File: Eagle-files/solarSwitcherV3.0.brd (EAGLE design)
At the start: 46.8 x 66.2 mm, 17 parts, among them T1 2N3440

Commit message: Started on version 3.0
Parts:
- added OK1: H11L1M, optocoupler:DIL06
- R1: value 10k -> 100k
- moved D2 52.8 mm to (32.2, 58.3), turned to 315 degrees
- moved U$5 1.75 mm to (19.1, 42.0)
- turned C1 to 90 degrees
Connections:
- removed net N$10: C1.-, GREEN_LED.K, JP2.GND, JP4.4, SV2.2, T1.1, U$5.IN
- new net N$15: C1.-, D1.A, GREEN_LED.K, JP2.GND, JP3.GND, JP4.4, SV2.2, T1.1, U$2.COIL1, U$5.IN
- new net N$17: D1.C, OK1.4, U$2.COIL0
- net N$12: now also OK1.1, OK1.5; no longer D1.C, U$2.COIL0
- net N$3: no longer D1.A, U$2.COIL1
- net VCC: now also OK1.6
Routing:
- net N$15: track 0.00 -> 107.4 mm
- net N$12: track 31.6 -> 2.65 mm
- net N$17: track 0.00 -> 20.8 mm
- net N$8: track 0.00 -> 18.3 mm
- net N$1: track 35.2 -> 37.0 mm

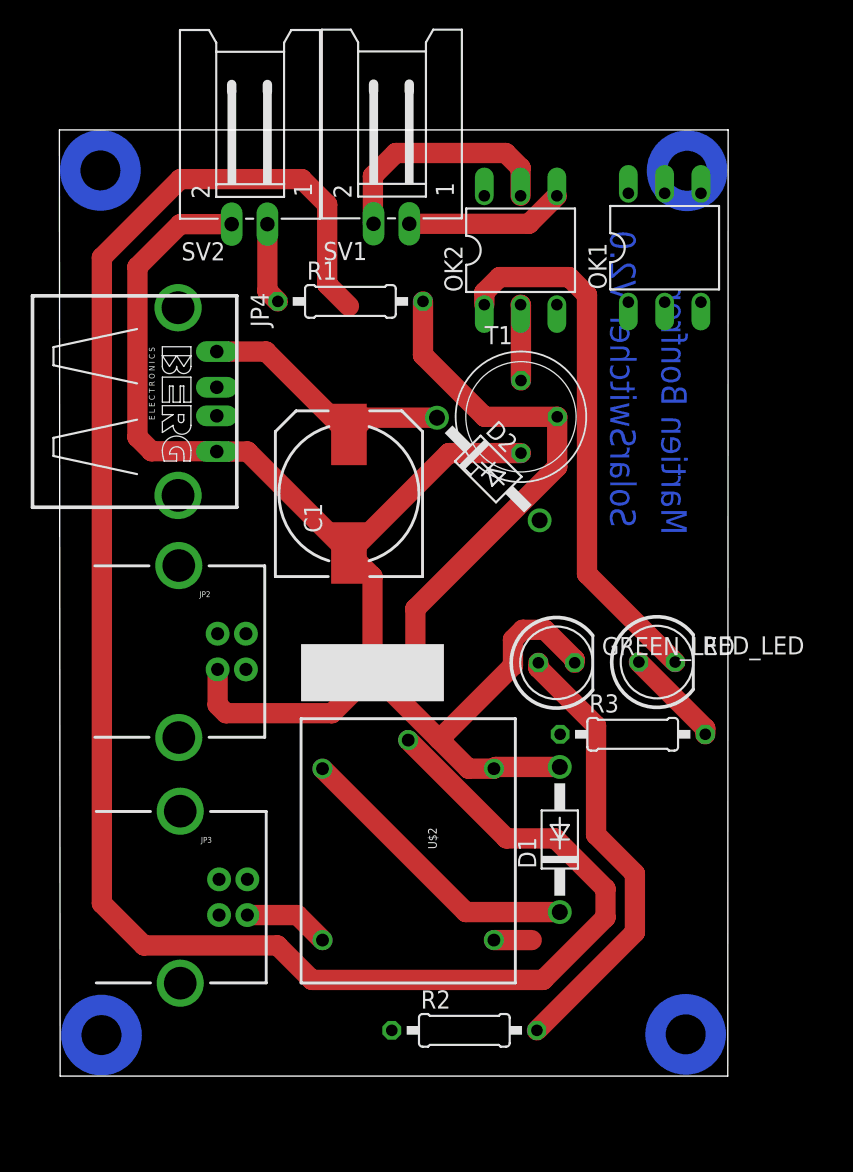
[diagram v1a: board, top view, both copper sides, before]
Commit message: Placed and connected all components
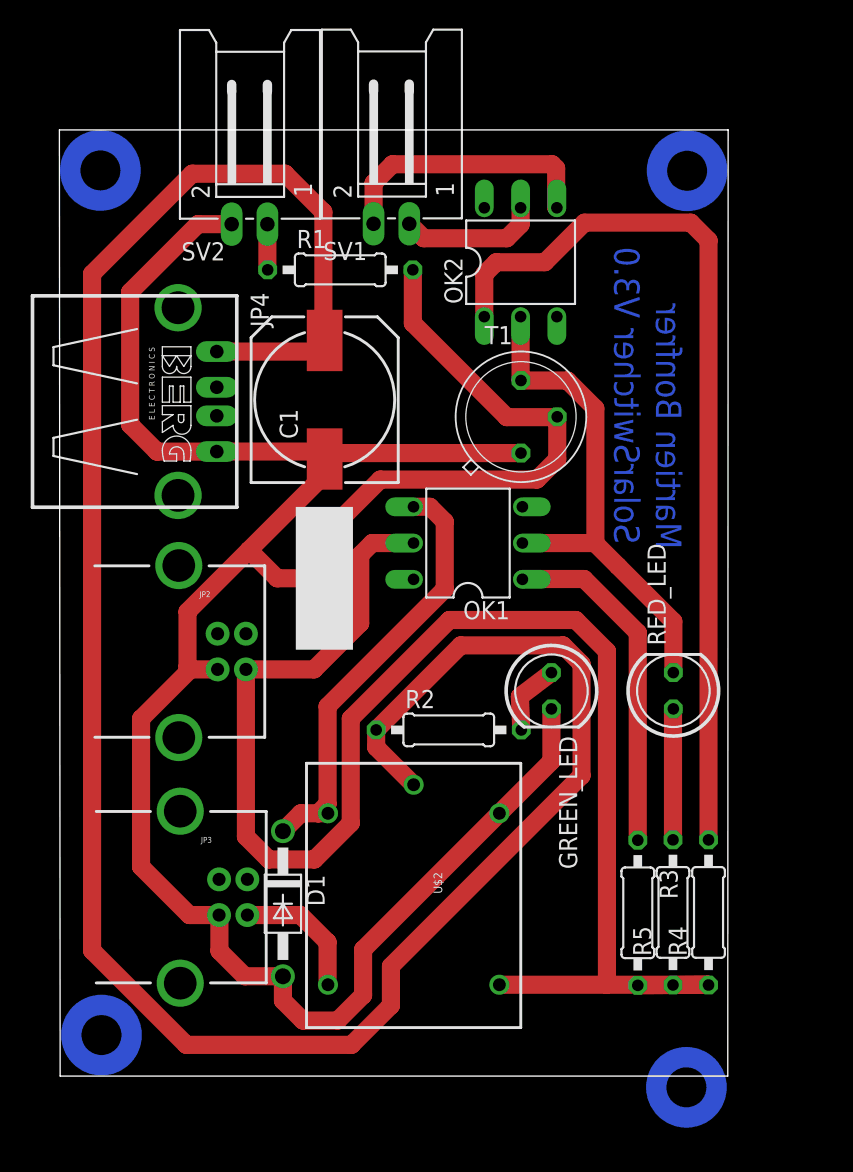
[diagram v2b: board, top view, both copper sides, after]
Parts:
- removed D2: 1N4004, diode:DO41-10
- added R4: 330, resistor:0207/10
- added R5: 150, resistor:0207/10
- R3: value 180 -> 330
- moved OK1 24.8 mm to (30.8, 53.1), turned to 90 degrees
- moved R2 21.1 mm to (29.5, 40.0)
- moved D1 19.9 mm to (17.9, 27.8), turned to 270 degrees
- moved R3 12.5 mm to (42.7, 27.2), turned to 270 degrees
- moved C1 6.80 mm to (20.8, 63.1)
- moved U$5 5.12 mm to (22.8, 45.6), turned to 90 degrees
- moved U$2 3.15 mm to (27.1, 28.8)
- moved R1 2.32 mm to (21.9, 72.2)
- moved RED_LED 2.31 mm to (45.2, 42.7), turned to 90 degrees
- moved GREEN_LED 1.99 mm to (36.7, 42.7), turned to 270 degrees
- moved OK2 0.84 mm to (34.5, 72.7)
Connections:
- removed net N$2: D2.A, R2.1, U$2.SWCOMMON
- new net N$18: OK1.1, R3.1
- net N$12: now also R3.2, R4.1, R5.1; no longer OK1.1
- net N$14: now also R5.2; no longer R3.2
- net N$3: now also R4.2; no longer R3.1, RED_LED.K
- net N$4: now also SV1.2; no longer SV1.1
- net N$7: now also SV1.1; no longer SV1.2
- net N$8: now also R2.1, U$2.SWCOMMON; no longer D2.C
- net N$9: now also OK1.2, RED_LED.K
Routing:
- net N$8: track 18.3 -> 162.3 mm
- net N$2: track 131.2 -> 0.00 mm
- net N$12: track 2.65 -> 110.9 mm
- net N$9: track 5.32 -> 36.4 mm
- net N$15: track 107.4 -> 137.9 mm
- net N$13: track 31.4 -> 5.11 mm
- net N$3: track 37.3 -> 62.6 mm
- net N$18: track 0.00 -> 24.2 mm
- net N$17: track 20.8 -> 30.4 mm
- net N$4: track 11.1 -> 19.1 mm
- net N$7: track 16.8 -> 9.78 mm
- net N$6: track 5.99 -> 9.39 mm
- net N$5: track 5.71 -> 3.21 mm
- net N$14: track 6.98 -> 9.18 mm
- net N$1: track 37.0 -> 38.1 mm
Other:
- board text added: "SolarSwitcher V3.0"
- board text removed: "SolarSwitcher V2.0"
